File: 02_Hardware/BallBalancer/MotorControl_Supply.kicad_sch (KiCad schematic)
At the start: 69 parts, among them J8 Jack-DC, M1 Motor_DC, M2 Motor_DC, Q1 DMN10H220L, Q2 DMN10H220L, Q3 DMN10H220L, Q4 DMN10H220L, Q5 DMN10H220L, Q6 DMN10H220L, Q7 DMN10H220L, Q8 DMN10H220L, U3 DGD0506A, U4 DGD0506A, U5 LM2937IMP5, U6 AP63203WU, U7 DGD0506A, U8 DGD0506A

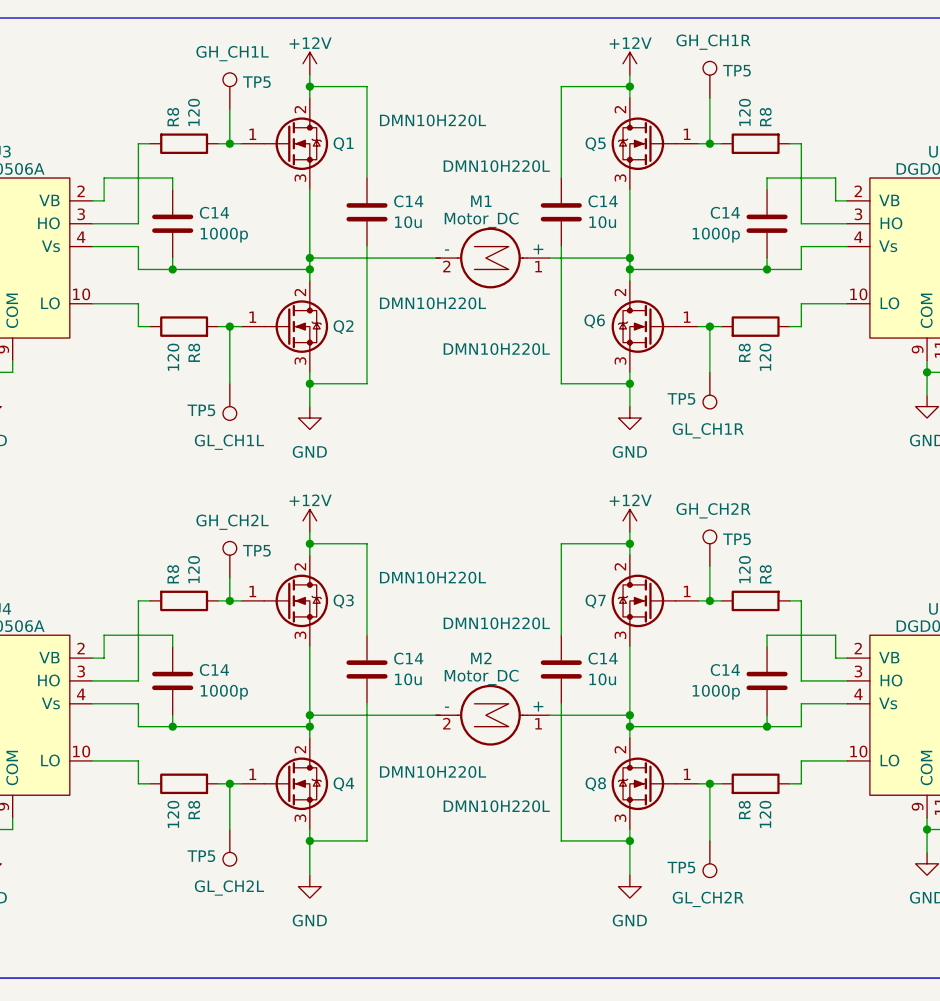
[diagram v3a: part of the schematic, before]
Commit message: Layout completed with stm32g431
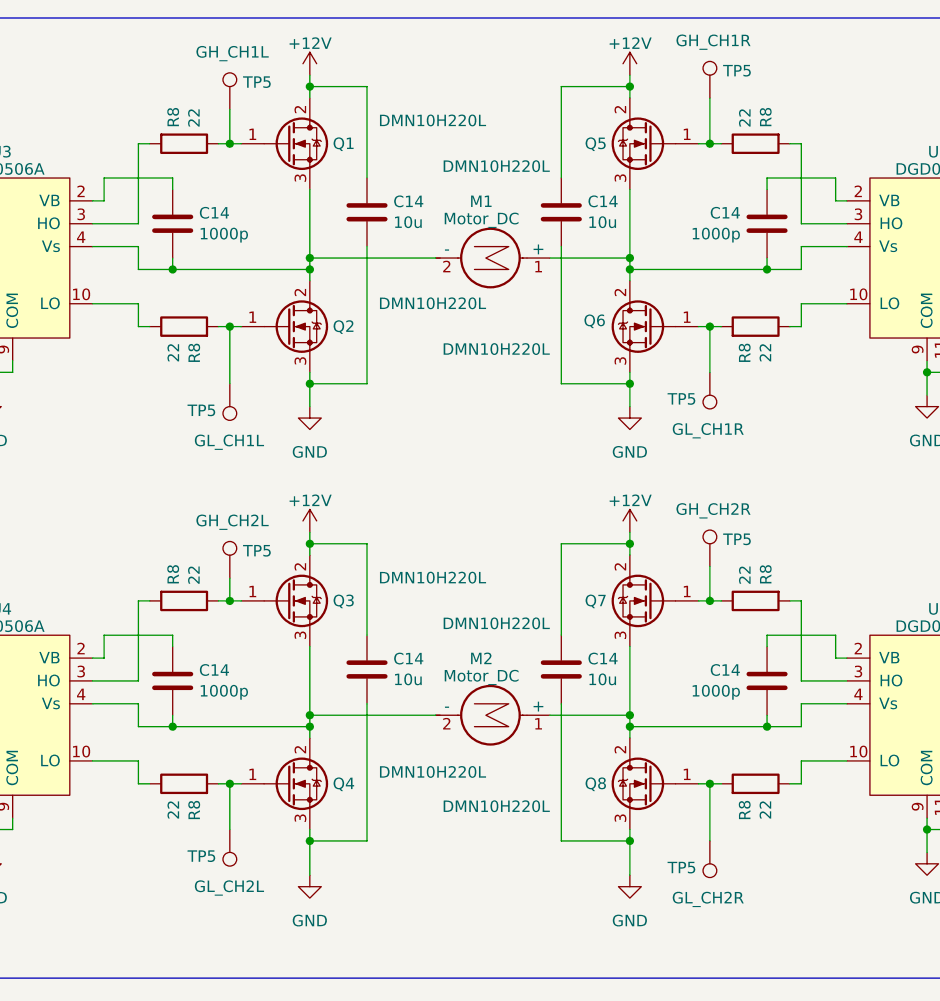
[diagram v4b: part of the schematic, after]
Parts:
- R8: value 120 -> 22; Hersteller Nr. CRCW0603120RFKEAC -> CRCW060322R0FKEAHP; Info 75V; 1%; 100mW; -55C; +155C -> 75V; 1%; 330mW; -55C; +155C; Mouser Nr. 71-CRCW0603120RFKEA -> 71-CRCW060322R0FKEAH
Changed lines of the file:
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@@
       (effects (font (size 1.27 1.27)) (justify right))
     )
-    (property "Value" "120" (at 93.853 27.432 0)
+    (property "Value" "22" (at 93.853 27.432 0)
       (effects (font (size 1.27 1.27)) (justify right))
     )
@@
       (effects (font (size 1.27 1.27)) hide)
     )
-    (property "Hersteller Nr." "CRCW0603120RFKEAC" (at 92.71 29.21 0)
-      (effects (font (size 1.27 1.27)) hide)
-    )
-    (property "Mouser Nr." "71-CRCW0603120RFKEA" (at 92.71 29.21 0)
-      (effects (font (size 1.27 1.27)) hide)
-    )
-    (property "Info" "75V; 1%; 100mW; -55C; +155C" (at 92.71 29.21 0)
+    (property "Hersteller Nr." "CRCW060322R0FKEAHP" (at 92.71 29.21 0)
+      (effects (font (size 1.27 1.27)) hide)
+    )
+    (property "Mouser Nr." "71-CRCW060322R0FKEAH" (at 92.71 29.21 0)
+      (effects (font (size 1.27 1.27)) hide)
+    )
+    (property "Info" "75V; 1%; 330mW; -55C; +155C" (at 92.71 29.21 0)
       (effects (font (size 1.27 1.27)) hide)
     )
@@
       (effects (font (size 1.27 1.27)) (justify right))
     )
-    (property "Value" "120" (at 91.567 51.308 0)
+    (property "Value" "22" (at 91.567 51.308 0)
       (effects (font (size 1.27 1.27)) (justify right))
     )
@@
       (effects (font (size 1.27 1.27)) hide)
     )
-    (property "Hersteller Nr." "CRCW0603120RFKEAC" (at 92.71 49.53 0)
-      (effects (font (size 1.27 1.27)) hide)
-    )
-    (property "Mouser Nr." "71-CRCW0603120RFKEA" (at 92.71 49.53 0)
-      (effects (font (size 1.27 1.27)) hide)
-    )
-    (property "Info" "75V; 1%; 100mW; -55C; +155C" (at 92.71 49.53 0)
+    (property "Hersteller Nr." "CRCW060322R0FKEAHP" (at 92.71 49.53 0)
+      (effects (font (size 1.27 1.27)) hide)
+    )
+    (property "Mouser Nr." "71-CRCW060322R0FKEAH" (at 92.71 49.53 0)
+      (effects (font (size 1.27 1.27)) hide)
+    )
+    (property "Info" "75V; 1%; 330mW; -55C; +155C" (at 92.71 49.53 0)
       (effects (font (size 1.27 1.27)) hide)
     )
@@
       (effects (font (size 1.27 1.27)) (justify right))
     )
-    (property "Value" "120" (at 157.353 102.108 0)
+    (property "Value" "22" (at 157.353 102.108 0)
       (effects (font (size 1.27 1.27)) (justify right))
     )
@@
       (effects (font (size 1.27 1.27)) hide)
     )
-    (property "Hersteller Nr." "CRCW0603120RFKEAC" (at 156.21 100.33 0)
-      (effects (font (size 1.27 1.27)) hide)
-    )
-    (property "Mouser Nr." "71-CRCW0603120RFKEA" (at 156.21 100.33 0)
-      (effects (font (size 1.27 1.27)) hide)
-    )
-    (property "Info" "75V; 1%; 100mW; -55C; +155C" (at 156.21 100.33 0)
+    (property "Hersteller Nr." "CRCW060322R0FKEAHP" (at 156.21 100.33 0)
+      (effects (font (size 1.27 1.27)) hide)
+    )
+    (property "Mouser Nr." "71-CRCW060322R0FKEAH" (at 156.21 100.33 0)
+      (effects (font (size 1.27 1.27)) hide)
+    )
+    (property "Info" "75V; 1%; 330mW; -55C; +155C" (at 156.21 100.33 0)
       (effects (font (size 1.27 1.27)) hide)
     )
@@
       (effects (font (size 1.27 1.27)) (justify right))
     )
-    (property "Value" "120" (at 157.353 51.308 0)
+    (property "Value" "22" (at 157.353 51.308 0)
       (effects (font (size 1.27 1.27)) (justify right))
     )
@@
       (effects (font (size 1.27 1.27)) hide)
     )
-    (property "Hersteller Nr." "CRCW0603120RFKEAC" (at 156.21 49.53 0)
-      (effects (font (size 1.27 1.27)) hide)
-    )
-    (property "Mouser Nr." "71-CRCW0603120RFKEA" (at 156.21 49.53 0)
-      (effects (font (size 1.27 1.27)) hide)
-    )
-    (property "Info" "75V; 1%; 100mW; -55C; +155C" (at 156.21 49.53 0)
+    (property "Hersteller Nr." "CRCW060322R0FKEAHP" (at 156.21 49.53 0)
+      (effects (font (size 1.27 1.27)) hide)
+    )
+    (property "Mouser Nr." "71-CRCW060322R0FKEAH" (at 156.21 49.53 0)
+      (effects (font (size 1.27 1.27)) hide)
+    )
+    (property "Info" "75V; 1%; 330mW; -55C; +155C" (at 156.21 49.53 0)
       (effects (font (size 1.27 1.27)) hide)
     )
@@
       (effects (font (size 1.27 1.27)) (justify right))
     )
-    (property "Value" "120" (at 155.067 78.232 0)
+    (property "Value" "22" (at 155.067 78.232 0)
       (effects (font (size 1.27 1.27)) (justify right))
     )
@@
       (effects (font (size 1.27 1.27)) hide)
     )
-    (property "Hersteller Nr." "CRCW0603120RFKEAC" (at 156.21 80.01 0)
-      (effects (font (size 1.27 1.27)) hide)
-    )
-    (property "Mouser Nr." "71-CRCW0603120RFKEA" (at 156.21 80.01 0)
-      (effects (font (size 1.27 1.27)) hide)
-    )
-    (property "Info" "75V; 1%; 100mW; -55C; +155C" (at 156.21 80.01 0)
+    (property "Hersteller Nr." "CRCW060322R0FKEAHP" (at 156.21 80.01 0)
+      (effects (font (size 1.27 1.27)) hide)
+    )
+    (property "Mouser Nr." "71-CRCW060322R0FKEAH" (at 156.21 80.01 0)
+      (effects (font (size 1.27 1.27)) hide)
+    )
+    (property "Info" "75V; 1%; 330mW; -55C; +155C" (at 156.21 80.01 0)
       (effects (font (size 1.27 1.27)) hide)
     )
@@
       (effects (font (size 1.27 1.27)) (justify right))
     )
-    (property "Value" "120" (at 93.853 78.232 0)
+    (property "Value" "22" (at 93.853 78.232 0)
       (effects (font (size 1.27 1.27)) (justify right))
     )
@@
       (effects (font (size 1.27 1.27)) hide)
     )
-    (property "Hersteller Nr." "CRCW0603120RFKEAC" (at 92.71 80.01 0)
-      (effects (font (size 1.27 1.27)) hide)
-    )
-    (property "Mouser Nr." "71-CRCW0603120RFKEA" (at 92.71 80.01 0)
-      (effects (font (size 1.27 1.27)) hide)
-    )
-    (property "Info" "75V; 1%; 100mW; -55C; +155C" (at 92.71 80.01 0)
+    (property "Hersteller Nr." "CRCW060322R0FKEAHP" (at 92.71 80.01 0)
+      (effects (font (size 1.27 1.27)) hide)
+    )
+    (property "Mouser Nr." "71-CRCW060322R0FKEAH" (at 92.71 80.01 0)
+      (effects (font (size 1.27 1.27)) hide)
+    )
+    (property "Info" "75V; 1%; 330mW; -55C; +155C" (at 92.71 80.01 0)
       (effects (font (size 1.27 1.27)) hide)
     )
@@
       (effects (font (size 1.27 1.27)) (justify right))
     )
-    (property "Value" "120" (at 91.567 102.108 0)
+    (property "Value" "22" (at 91.567 102.108 0)
       (effects (font (size 1.27 1.27)) (justify right))
     )
@@
       (effects (font (size 1.27 1.27)) hide)
     )
-    (property "Hersteller Nr." "CRCW0603120RFKEAC" (at 92.71 100.33 0)
-      (effects (font (size 1.27 1.27)) hide)
-    )
-    (property "Mouser Nr." "71-CRCW0603120RFKEA" (at 92.71 100.33 0)
-      (effects (font (size 1.27 1.27)) hide)
-    )
-    (property "Info" "75V; 1%; 100mW; -55C; +155C" (at 92.71 100.33 0)
+    (property "Hersteller Nr." "CRCW060322R0FKEAHP" (at 92.71 100.33 0)
+      (effects (font (size 1.27 1.27)) hide)
+    )
+    (property "Mouser Nr." "71-CRCW060322R0FKEAH" (at 92.71 100.33 0)
+      (effects (font (size 1.27 1.27)) hide)
+    )
+    (property "Info" "75V; 1%; 330mW; -55C; +155C" (at 92.71 100.33 0)
       (effects (font (size 1.27 1.27)) hide)
     )
@@
       (effects (font (size 1.27 1.27)) (justify right))
     )
-    (property "Value" "120" (at 155.067 27.432 0)
+    (property "Value" "22" (at 155.067 27.432 0)
       (effects (font (size 1.27 1.27)) (justify right))
     )
@@
       (effects (font (size 1.27 1.27)) hide)
     )
-    (property "Hersteller Nr." "CRCW0603120RFKEAC" (at 156.21 29.21 0)
-      (effects (font (size 1.27 1.27)) hide)
-    )
-    (property "Mouser Nr." "71-CRCW0603120RFKEA" (at 156.21 29.21 0)
-      (effects (font (size 1.27 1.27)) hide)
-    )
-    (property "Info" "75V; 1%; 100mW; -55C; +155C" (at 156.21 29.21 0)
-      (effects (font (size 1.27 1.27)) hide)
-    )
+    (property "Hersteller Nr." "CRCW060322R0FKEAHP" (at 156.21 29.21 0)
+      (effects (font (size 1.27 1.27)) hide)
+    )
+    (property "Mouser Nr." "71-CRCW060322R0FKEAH" (at 156.21 29.21 0)
+      (effects (font (size 1.27 1.27)) hide)
+    )
+    (property "Info" "75V; 1%; 330mW; -55C; +155C" (at 156.21 29.21 0)
+      (effects (font (size 1.27 1.27)) hide)
+    )
